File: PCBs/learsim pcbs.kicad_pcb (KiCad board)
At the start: 2 copper layers, 11 parts, among them U1 ESP32-C6-DEV-KIT-N8, U2 MAX7219, U3 MAX7219

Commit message: pcb work
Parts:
- added D1: COM1, LED_SMD:LED_SK6812MINI-E_3.2x2.8mm_P1.5mm_ReverseMount, B.Cu at (32.5, 120.5)
- added D2: COM2, LED_SMD:LED_SK6812MINI-E_3.2x2.8mm_P1.5mm_ReverseMount, B.Cu at (57.0, 120.4)
- added D3: NAV1, LED_SMD:LED_SK6812MINI-E_3.2x2.8mm_P1.5mm_ReverseMount, B.Cu at (82.0, 120.4)
- added D4: NAV2, LED_SMD:LED_SK6812MINI-E_3.2x2.8mm_P1.5mm_ReverseMount, B.Cu at (107.3, 120.2)
- added D5: Switch1, LED_SMD:LED_SK6812MINI-E_3.2x2.8mm_P1.5mm_ReverseMount, B.Cu at (50.8, 74.0)
- added D6: ADF1, LED_SMD:LED_SK6812MINI-E_3.2x2.8mm_P1.5mm_ReverseMount, B.Cu at (131.5, 120.3)
- added SW1: MHz, Rotary:SW-TH_EC12EXXXX, F.Cu at (97.7, 72.5)
- added SW2: KHz, Rotary:SW-TH_EC12EXXXX, F.Cu at (129.2, 72.5)
- U1: footprint esppico:ESP32-C6-Pico -> ESP32-Pico:ESP32-C6-Pico
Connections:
- U1 pad 13: unconnected-(U1-GPIO21-Pad13) -> Net-(D1-DIN)
- U1 pad 16: unconnected-(U1-Vbus-Pad16) -> +5V
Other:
- board outline added: 120 x 110 mm

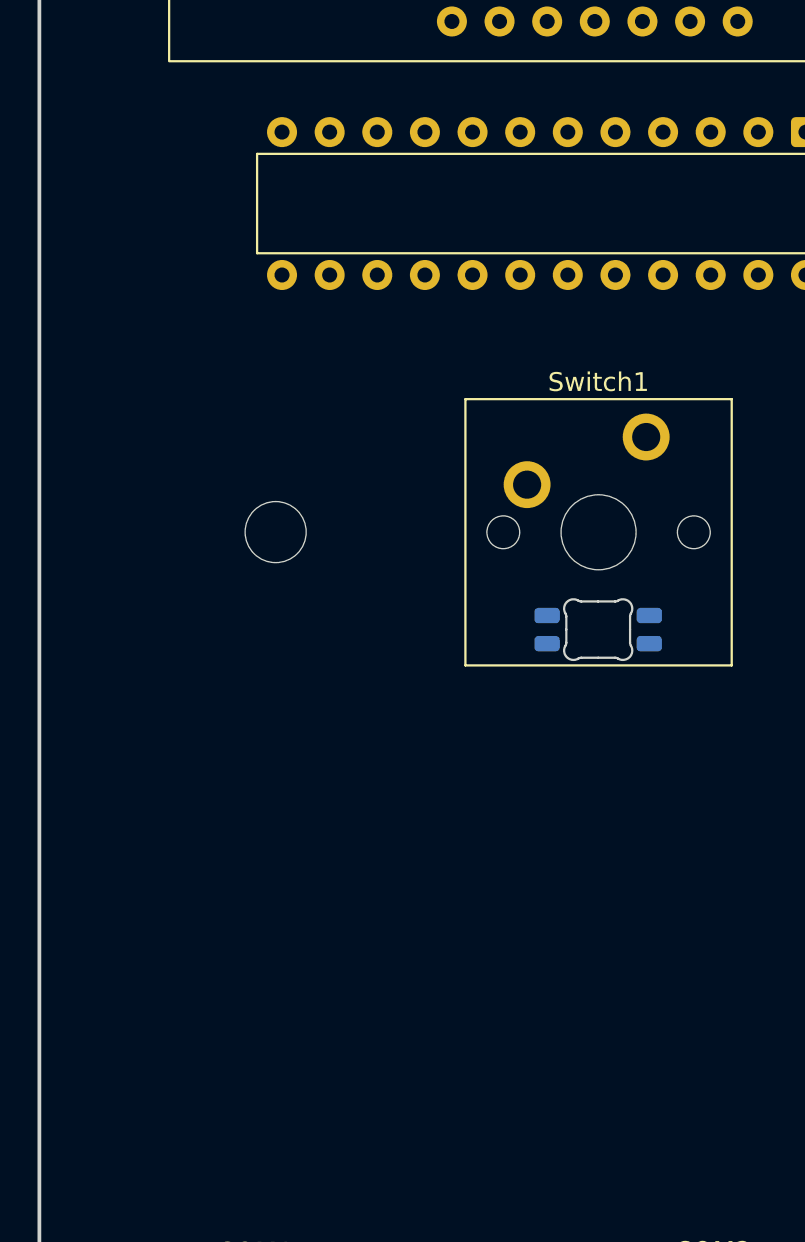
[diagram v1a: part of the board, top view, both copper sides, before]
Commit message: Add new toggle switch symbol and footprint for 1FS1T1B9M2RES-5
- Created a new symbol for the toggle switch 1FS1T1B9M2RES-5 in the easyeda2kicad library, including properties such as reference, value, footprint, datasheet, manufacturer, MPN, and LCSC part number.
- Added a corresponding footprint module for the toggle switch, defining pads, silk screen, and 3D model for better visualization in PCB design.
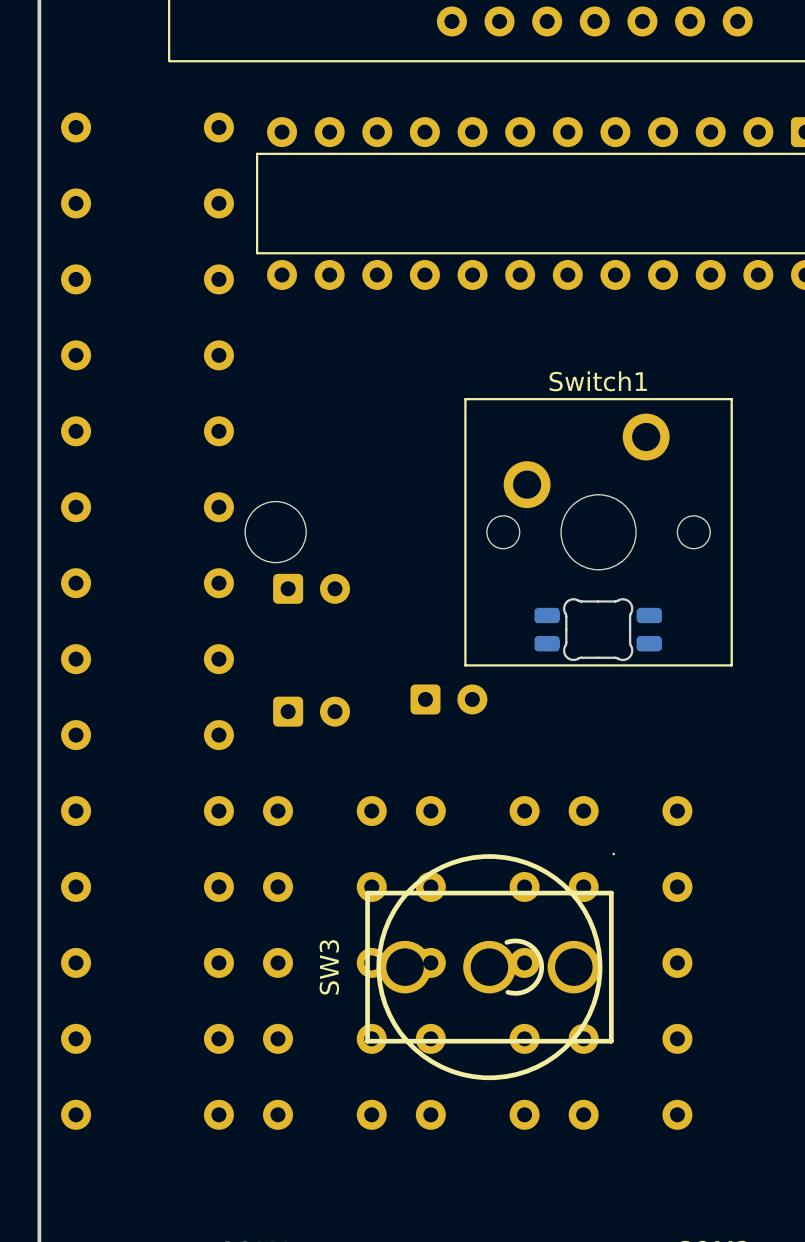
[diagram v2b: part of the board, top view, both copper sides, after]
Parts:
- added C1: 10uF, Capacitor_THT:CP_Radial_D5.0mm_P2.50mm, B.Cu at (34.3, 78.4)
- added C10: 100nF, Capacitor_THT:C_Disc_D5.0mm_W2.5mm_P5.00mm, B.Cu at (41.9, 95.8)
- added C11: 100nF, Capacitor_THT:C_Disc_D5.0mm_W2.5mm_P5.00mm, B.Cu at (41.9, 91.8)
- added C12: 100nF, Capacitor_THT:C_Disc_D5.0mm_W2.5mm_P5.00mm, B.Cu at (41.9, 87.7)
- added C13: 100nF, Capacitor_THT:C_Disc_D5.0mm_W2.5mm_P5.00mm, B.Cu at (41.9, 83.7)
- added C14: 100nF, Capacitor_THT:C_Disc_D5.0mm_W2.5mm_P5.00mm, B.Cu at (50.0, 99.9)
- added C15: 100nF, Capacitor_THT:C_Disc_D5.0mm_W2.5mm_P5.00mm, B.Cu at (50.0, 95.8)
- added C16: 100nF, Capacitor_THT:C_Disc_D5.0mm_W2.5mm_P5.00mm, B.Cu at (50.0, 91.8)
- added C17: 100nF, Capacitor_THT:C_Disc_D5.0mm_W2.5mm_P5.00mm, B.Cu at (50.0, 87.7)
- added C18: 100nF, Capacitor_THT:C_Disc_D5.0mm_W2.5mm_P5.00mm, B.Cu at (50.0, 83.7)
- added C2: 100nF, Capacitor_THT:C_Disc_D5.0mm_W2.5mm_P5.00mm, B.Cu at (33.7, 99.9)
- added C3: 10uF, Capacitor_THT:CP_Radial_D5.0mm_P2.50mm, B.Cu at (34.3, 71.8)
- added C4: 100nF, Capacitor_THT:C_Disc_D5.0mm_W2.5mm_P5.00mm, B.Cu at (33.7, 95.8)
- added C5: 100nF, Capacitor_THT:C_Disc_D5.0mm_W2.5mm_P5.00mm, B.Cu at (33.7, 91.8)
- added C6: 100uF, Capacitor_THT:CP_Radial_D6.3mm_P2.50mm, B.Cu at (41.6, 77.7)
- added C7: 100nF, Capacitor_THT:C_Disc_D5.0mm_W2.5mm_P5.00mm, B.Cu at (33.7, 87.7)
- added C8: 100nF, Capacitor_THT:C_Disc_D5.0mm_W2.5mm_P5.00mm, B.Cu at (33.7, 83.7)
- added C9: 100nF, Capacitor_THT:C_Disc_D5.0mm_W2.5mm_P5.00mm, B.Cu at (41.9, 99.9)
- added R1: 33k, Resistor_THT:R_Axial_DIN0207_L6.3mm_D2.5mm_P7.62mm_Horizontal, B.Cu at (23.0, 99.9)
- added R10: 10k, Resistor_THT:R_Axial_DIN0207_L6.3mm_D2.5mm_P7.62mm_Horizontal, B.Cu at (23.0, 63.4)
- added R11: 10k, Resistor_THT:R_Axial_DIN0207_L6.3mm_D2.5mm_P7.62mm_Horizontal, B.Cu at (23.0, 59.4)
- added R12: 10k, Resistor_THT:R_Axial_DIN0207_L6.3mm_D2.5mm_P7.62mm_Horizontal, B.Cu at (23.0, 55.3)
- added R13: 10k, Resistor_THT:R_Axial_DIN0207_L6.3mm_D2.5mm_P7.62mm_Horizontal, B.Cu at (23.0, 51.3)
- added R14: 10k, Resistor_THT:R_Axial_DIN0207_L6.3mm_D2.5mm_P7.62mm_Horizontal, B.Cu at (23.0, 47.2)
- added R2: 33k, Resistor_THT:R_Axial_DIN0207_L6.3mm_D2.5mm_P7.62mm_Horizontal, B.Cu at (23.0, 95.8)
- added R3: 10k, Resistor_THT:R_Axial_DIN0207_L6.3mm_D2.5mm_P7.62mm_Horizontal, B.Cu at (23.0, 91.8)
- added R4: 10k, Resistor_THT:R_Axial_DIN0207_L6.3mm_D2.5mm_P7.62mm_Horizontal, B.Cu at (23.0, 87.7)
- added R5: 10k, Resistor_THT:R_Axial_DIN0207_L6.3mm_D2.5mm_P7.62mm_Horizontal, B.Cu at (23.0, 83.7)
- added R6: 10k, Resistor_THT:R_Axial_DIN0207_L6.3mm_D2.5mm_P7.62mm_Horizontal, B.Cu at (23.0, 79.6)
- added R7: 10k, Resistor_THT:R_Axial_DIN0207_L6.3mm_D2.5mm_P7.62mm_Horizontal, B.Cu at (23.0, 75.6)
- added R8: 10k, Resistor_THT:R_Axial_DIN0207_L6.3mm_D2.5mm_P7.62mm_Horizontal, B.Cu at (23.0, 71.5)
- added R9: 10k, Resistor_THT:R_Axial_DIN0207_L6.3mm_D2.5mm_P7.62mm_Horizontal, B.Cu at (23.0, 67.5)
- added SW3: 1FS1T1B9M2RES-5, Rotary:SW-TH_1FS1T1B9M2RES-5, F.Cu at (45.0, 92.0)
- DS1, DS2: footprint 7segment:LED-6DIGIT-0.36in-CC_14P -> 7-Segment Display:LED-6DIGIT-0.36in-CC_14P
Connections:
- net Net-(D1-DIN) renamed LED_DIN
- net Net-(D1-DOUT) renamed LED_12
- net Net-(D2-DOUT) renamed LED_23
- net Net-(D3-DOUT) renamed LED_34
- net Net-(D4-DOUT) renamed LED_45
- net Net-(D5-DOUT) renamed LED_56
- ADF1 pad 2: unconnected-(ADF1-Pad2) -> BTN_ADF1
- COM1 pad 2: unconnected-(COM1-Pad2) -> BTN_COM1
- COM2 pad 2: unconnected-(COM2-Pad2) -> BTN_COM2
- DS1 pad 1: unconnected-(DS1-D-Pad1) -> U3_SEG_D
- DS1 pad 10: unconnected-(DS1-F-Pad10) -> U3_SEG_F
- DS1 pad 11: unconnected-(DS1-A-Pad11) -> U3_SEG_A
- DS1 pad 12: unconnected-(DS1-DIG3-Pad12) -> U3_DIG2
- DS1 pad 13: unconnected-(DS1-DIG2-Pad13) -> U3_DIG1
- DS1 pad 14: unconnected-(DS1-DIG1-Pad14) -> U3_DIG0
- DS1 pad 2: unconnected-(DS1-DP-Pad2) -> U3_SEG_DP
- DS1 pad 3: unconnected-(DS1-E-Pad3) -> U3_SEG_E
- DS1 pad 4: unconnected-(DS1-C-Pad4) -> U3_SEG_C
- DS1 pad 5: unconnected-(DS1-DIG6-Pad5) -> U3_DIG5
- DS1 pad 6: unconnected-(DS1-G-Pad6) -> U3_SEG_G
- DS1 pad 7: unconnected-(DS1-B-Pad7) -> U3_SEG_B
- DS1 pad 8: unconnected-(DS1-DIG5-Pad8) -> U3_DIG4
- DS1 pad 9: unconnected-(DS1-DIG4-Pad9) -> U3_DIG3
- DS2 pad 1: unconnected-(DS2-D-Pad1) -> U2_SEG_D
- DS2 pad 10: unconnected-(DS2-F-Pad10) -> U2_SEG_F
- DS2 pad 11: unconnected-(DS2-A-Pad11) -> U2_SEG_A
- DS2 pad 12: unconnected-(DS2-DIG3-Pad12) -> U2_DIG2
- DS2 pad 13: unconnected-(DS2-DIG2-Pad13) -> U2_DIG1
- DS2 pad 14: unconnected-(DS2-DIG1-Pad14) -> U2_DIG0
- DS2 pad 2: unconnected-(DS2-DP-Pad2) -> U2_SEG_DP
- DS2 pad 3: unconnected-(DS2-E-Pad3) -> U2_SEG_E
- DS2 pad 4: unconnected-(DS2-C-Pad4) -> U2_SEG_C
- DS2 pad 5: unconnected-(DS2-DIG6-Pad5) -> U2_DIG5
- DS2 pad 6: unconnected-(DS2-G-Pad6) -> U2_SEG_G
- DS2 pad 7: unconnected-(DS2-B-Pad7) -> U2_SEG_B
- DS2 pad 8: unconnected-(DS2-DIG5-Pad8) -> U2_DIG4
- DS2 pad 9: unconnected-(DS2-DIG4-Pad9) -> U2_DIG3
- NAV1 pad 2: unconnected-(NAV1-Pad2) -> BTN_NAV1
- NAV2 pad 2: unconnected-(NAV2-Pad2) -> BTN_NAV2
- SW1 pad A: unconnected-(SW1-PadA) -> ENC1_A
- SW1 pad B: unconnected-(SW1-PadB) -> ENC1_B
- SW1 pad C: unconnected-(SW1-PadC) -> GND
- SW1 pad D: unconnected-(SW1-PadD) -> ENC1_SW
- SW1 pad E: unconnected-(SW1-PadE) -> GND
- SW2 pad A: unconnected-(SW2-PadA) -> ENC2_A
- SW2 pad B: unconnected-(SW2-PadB) -> ENC2_B
- SW2 pad C: unconnected-(SW2-PadC) -> GND
- SW2 pad D: unconnected-(SW2-PadD) -> ENC2_SW
- SW2 pad E: unconnected-(SW2-PadE) -> GND
- Switch1 pad 2: unconnected-(Switch1-Pad2) -> BTN_Switch1
- U1 pad 10: unconnected-(U1-GPIO16-Pad10) -> ENC1_B
- U1 pad 11: unconnected-(U1-GPIO18-Pad11) -> ENC2_A
- U1 pad 12: unconnected-(U1-GPIO20-Pad12) -> ENC2_SW
- U1 pad 14: unconnected-(U1-EXIO6-Pad14) -> BTN_Switch1
- U1 pad 17: unconnected-(U1-Vsys-Pad17) -> +5V
- U1 pad 19: unconnected-(U1-3V3-Pad19) -> +3V3
- U1 pad 22: unconnected-(U1-GPIO19-Pad22) -> ENC2_B
- U1 pad 26: unconnected-(U1-EXIO1-Pad26) -> BTN_COM1
- U1 pad 27: unconnected-(U1-EXIO2-Pad27) -> BTN_COM2
- U1 pad 28: unconnected-(U1-EXIO3-Pad28) -> BTN_NAV1
- U1 pad 29: unconnected-(U1-EXIO4-Pad29) -> BTN_NAV2
- U1 pad 30: unconnected-(U1-EXIO5-Pad30) -> BTN_ADF1
- U1 pad 4: unconnected-(U1-GPIO4-Pad4) -> SPI_LOAD
- U1 pad 5: unconnected-(U1-GPIO5-Pad5) -> ENC1_SW
- U1 pad 6: unconnected-(U1-GPIO6-Pad6) -> MAX_CHAIN
- U1 pad 7: unconnected-(U1-GPIO7-Pad7) -> SPI_CLK
- U1 pad 9: unconnected-(U1-GPIO15-Pad9) -> ENC1_A
- U2 pad 1: unconnected-(U2-DIN-Pad1) -> MAX_CHAIN
- U2 pad 10: unconnected-(U2-DIG_5-Pad10) -> U2_DIG5
- U2 pad 11: unconnected-(U2-DIG_1-Pad11) -> U2_DIG1
- U2 pad 12: unconnected-(U2-LOAD-Pad12) -> SPI_LOAD
- U2 pad 13: unconnected-(U2-CLK-Pad13) -> SPI_CLK
- U2 pad 14: unconnected-(U2-SEG_A-Pad14) -> U2_SEG_A
- U2 pad 15: unconnected-(U2-SEG_F-Pad15) -> U2_SEG_F
- U2 pad 16: unconnected-(U2-SEG_B-Pad16) -> U2_SEG_B
- U2 pad 17: unconnected-(U2-SEG_G-Pad17) -> U2_SEG_G
- U2 pad 19: unconnected-(U2-V+-Pad19) -> GND
- U2 pad 2: unconnected-(U2-DIG_0-Pad2) -> U2_DIG0
- U2 pad 20: unconnected-(U2-SEG_C-Pad20) -> U2_SEG_C
- U2 pad 21: unconnected-(U2-SEG_E-Pad21) -> U2_SEG_E
- U2 pad 22: unconnected-(U2-SEG_DP-Pad22) -> U2_SEG_DP
- U2 pad 23: unconnected-(U2-SEG_D-Pad23) -> U2_SEG_D
- U2 pad 24: unconnected-(U2-DOUT-Pad24) -> U2_ISET
- U2 pad 3: unconnected-(U2-DIG_4-Pad3) -> U2_DIG4
- U2 pad 4: Net-(U2-GND-Pad4) -> +5V
- U2 pad 6: unconnected-(U2-DIG_2-Pad6) -> U2_DIG2
- U2 pad 7: unconnected-(U2-DIG_3-Pad7) -> U2_DIG3
- U2 pad 9: Net-(U2-GND-Pad4) -> +5V
- U3 pad 1: unconnected-(U3-DIN-Pad1) -> MAX_CHAIN
- U3 pad 10: unconnected-(U3-DIG_5-Pad10) -> U3_DIG5
- U3 pad 11: unconnected-(U3-DIG_1-Pad11) -> U3_DIG1
- U3 pad 12: unconnected-(U3-LOAD-Pad12) -> SPI_LOAD
- U3 pad 13: unconnected-(U3-CLK-Pad13) -> SPI_CLK
- U3 pad 14: unconnected-(U3-SEG_A-Pad14) -> U3_SEG_A
- U3 pad 15: unconnected-(U3-SEG_F-Pad15) -> U3_SEG_F
- U3 pad 16: unconnected-(U3-SEG_B-Pad16) -> U3_SEG_B
- U3 pad 17: unconnected-(U3-SEG_G-Pad17) -> U3_SEG_G
- U3 pad 18: unconnected-(U3-ISET-Pad18) -> U3_ISET
- U3 pad 19: unconnected-(U3-V+-Pad19) -> GND
- U3 pad 2: unconnected-(U3-DIG_0-Pad2) -> U3_DIG0
- U3 pad 20: unconnected-(U3-SEG_C-Pad20) -> U3_SEG_C
- U3 pad 21: unconnected-(U3-SEG_E-Pad21) -> U3_SEG_E
- U3 pad 22: unconnected-(U3-SEG_DP-Pad22) -> U3_SEG_DP
- U3 pad 23: unconnected-(U3-SEG_D-Pad23) -> U3_SEG_D
- U3 pad 3: unconnected-(U3-DIG_4-Pad3) -> U3_DIG4
- U3 pad 4: Net-(U3-GND-Pad4) -> +5V
- U3 pad 6: unconnected-(U3-DIG_2-Pad6) -> U3_DIG2
- U3 pad 7: unconnected-(U3-DIG_3-Pad7) -> U3_DIG3
- U3 pad 9: Net-(U3-GND-Pad4) -> +5V

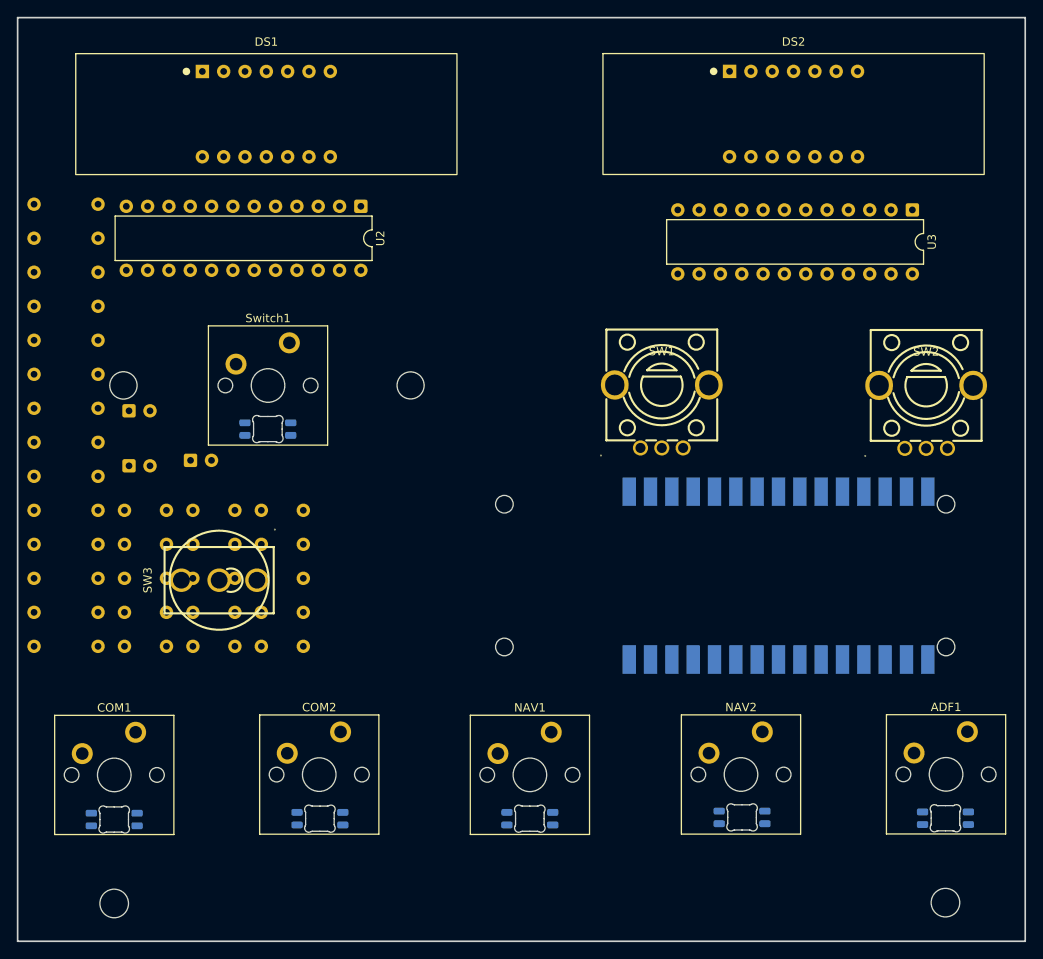
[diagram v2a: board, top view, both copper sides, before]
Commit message: Add new toggle switch symbols and footprints for 2MD3T1B1M2QES-5 and 2MS1T1B1M2QES-5
- Created symbol for 2MD3T1B1M2QES-5 with properties including reference, value, footprint, datasheet, manufacturer, MPN, and LCSC part.
- Added graphical representation including pins and connections for 2MD3T1B1M2QES-5.
- Created symbol for 2MS1T1B1M2QES-5 with similar properties and graphical representation.
- Added corresponding footprints for both switches in the KiCad library.
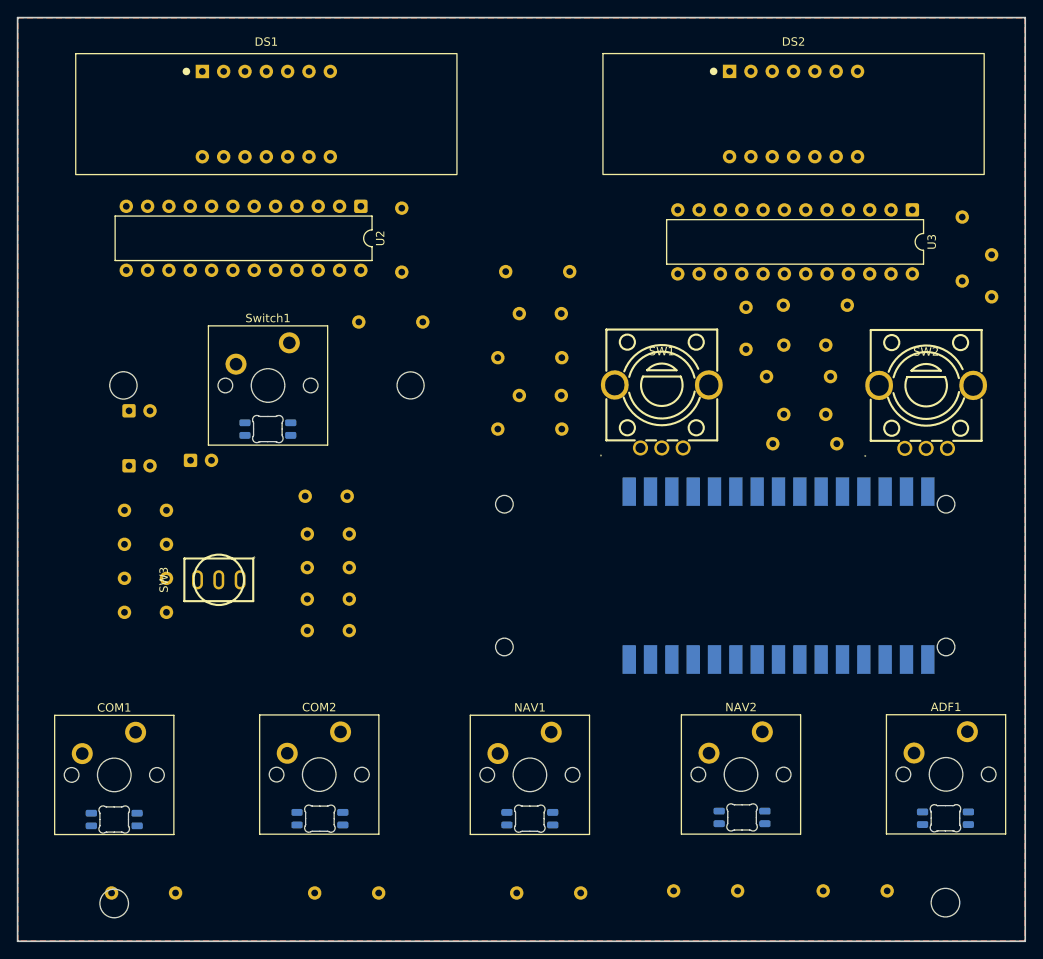
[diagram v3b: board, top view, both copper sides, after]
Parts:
- SW3: value 1FS1T1B9M2RES-5 -> 2MS1T1B1M2QES-5; footprint Rotary:SW-TH_1FS1T1B9M2RES-5 -> Rotary:SW-TH_2MS1T1B1M2QES-5
- moved R14 110.6 mm to (133.5, 48.8), turned to -90 degrees
- moved R7 108.1 mm to (116.9, 129.0)
- moved R2 96.4 mm to (112.2, 59.2)
- moved R6 90.8 mm to (99.1, 129.0)
- moved C18 90.6 mm to (137.0, 58.2), turned to 90 degrees
- moved R12 90.3 mm to (110.9, 75.8)
- moved R13 88.8 mm to (110.2, 67.8)
- moved R5 73.4 mm to (80.4, 129.2)
- moved C17 71.3 mm to (117.2, 64.0), turned to 180 degrees
- moved C16 70.0 mm to (117.2, 72.2), turned to 180 degrees
- moved C15 65.7 mm to (107.8, 64.5), turned to 90 degrees
- moved R1 62.5 mm to (66.8, 55.3), turned to 90 degrees
- moved R11 56.3 mm to (79.1, 55.2)
- moved R9 55.6 mm to (78.2, 74.0)
- moved R10 55.3 mm to (78.2, 65.5)
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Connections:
- U2 pad 18: unconnected-(U2-ISET-Pad18) -> U2_ISET
- U2 pad 24: U2_ISET -> unconnected-(U2-DOUT-Pad24)
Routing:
- added copper zone on F.Cu, net GND

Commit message: Remove unused global labels and a capacitor symbol from the schematic. Adjust positions of rotary switch properties for better alignment.
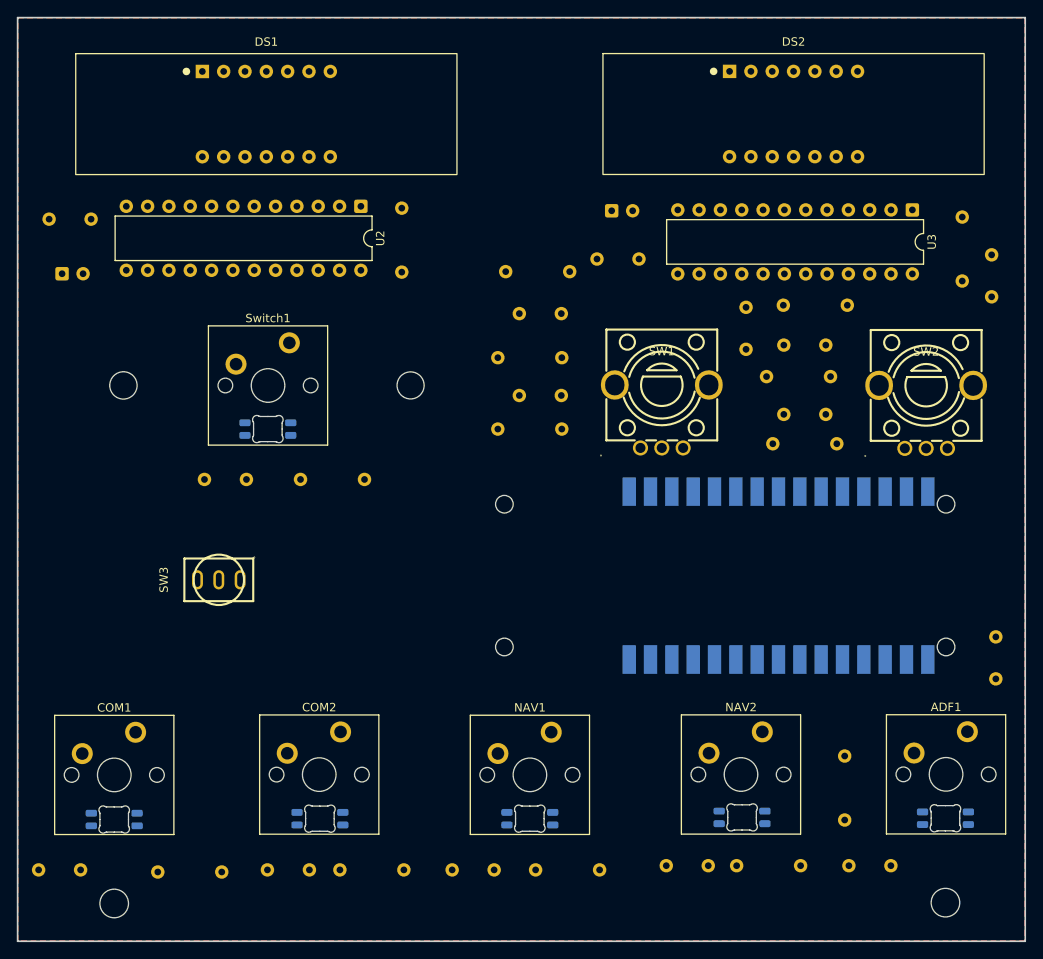
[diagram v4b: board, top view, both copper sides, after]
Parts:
- removed C6: 100uF, Capacitor_THT:CP_Radial_D6.3mm_P2.50mm
- moved C4 104.1 mm to (137.5, 103.8), turned to 90 degrees
- moved C12 78.3 mm to (120.0, 126.0)
- moved C5 67.9 mm to (90.0, 53.8)
- moved C1 65.0 mm to (91.8, 48.0)
- moved C10 55.6 mm to (98.2, 126.0)
- moved C11 51.2 mm to (23.5, 126.5)
- moved C7 39.8 mm to (24.8, 49.0)
- moved C9 36.6 mm to (72.8, 126.5)
- moved C2 28.9 mm to (50.8, 126.5)
- moved R8 20.0 mm to (62.3, 80.0)
- moved C3 18.2 mm to (26.3, 55.5)
- moved R7 16.3 mm to (119.5, 112.9), turned to -90 degrees
- moved C8 10.2 mm to (43.2, 80.0)
- moved R6 8.08 mm to (106.6, 126.0)
- moved R3 6.04 mm to (37.7, 126.8)
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
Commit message: Add multiple global labels and resistors to the learsim PCBs schematic
- Introduced new global labels: SW3_A, SW3_B, and GND at various coordinates.
- Added resistors R15 and R16 with specified properties and footprints.
- Ensured all new components have appropriate UUIDs and intersheet references.
- Adjusted existing global labels for consistency and clarity.
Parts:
- added R15: 10k, Resistor_THT:R_Axial_DIN0207_L6.3mm_D2.5mm_P7.62mm_Horizontal, F.Cu at (49.3, 97.5)
- added R16: 10k, Resistor_THT:R_Axial_DIN0207_L6.3mm_D2.5mm_P7.62mm_Horizontal, F.Cu at (41.6, 97.5)
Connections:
- SW3 pad 1: unconnected-(SW3-Pad1) -> SW3_A
- SW3 pad 2: unconnected-(SW3-Pad2) -> GND
- SW3 pad 3: unconnected-(SW3-Pad3) -> SW3_B
- U1 pad 20: unconnected-(U1-GPIO8-Pad20) -> SW3_A
- U1 pad 21: unconnected-(U1-GPIO9-Pad21) -> SW3_B
- U1 pad 6: MAX_CHAIN -> SPI_DIN
- U2 pad 1: MAX_CHAIN -> SPI_DIN
- U2 pad 19: GND -> +5V
- U2 pad 24: unconnected-(U2-DOUT-Pad24) -> MAX_CHAIN
- U2 pad 4: +5V -> GND
- U2 pad 9: +5V -> GND
- U3 pad 19: GND -> +5V
- U3 pad 4: +5V -> GND
- U3 pad 9: +5V -> GND
